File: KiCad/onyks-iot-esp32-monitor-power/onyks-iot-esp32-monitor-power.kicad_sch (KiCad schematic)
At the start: 42 parts, among them J1 Uart_con, J2 Jtag_con, J3 Conn_01x06, J4 Screw_Terminal_01x01, J5 Screw_Terminal_01x01, J6 Screw_Terminal_01x02, J7 Conn_01x02, K1 SANYOU_SRD_Form_C, Q1 SS8050, Q2 SS8050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

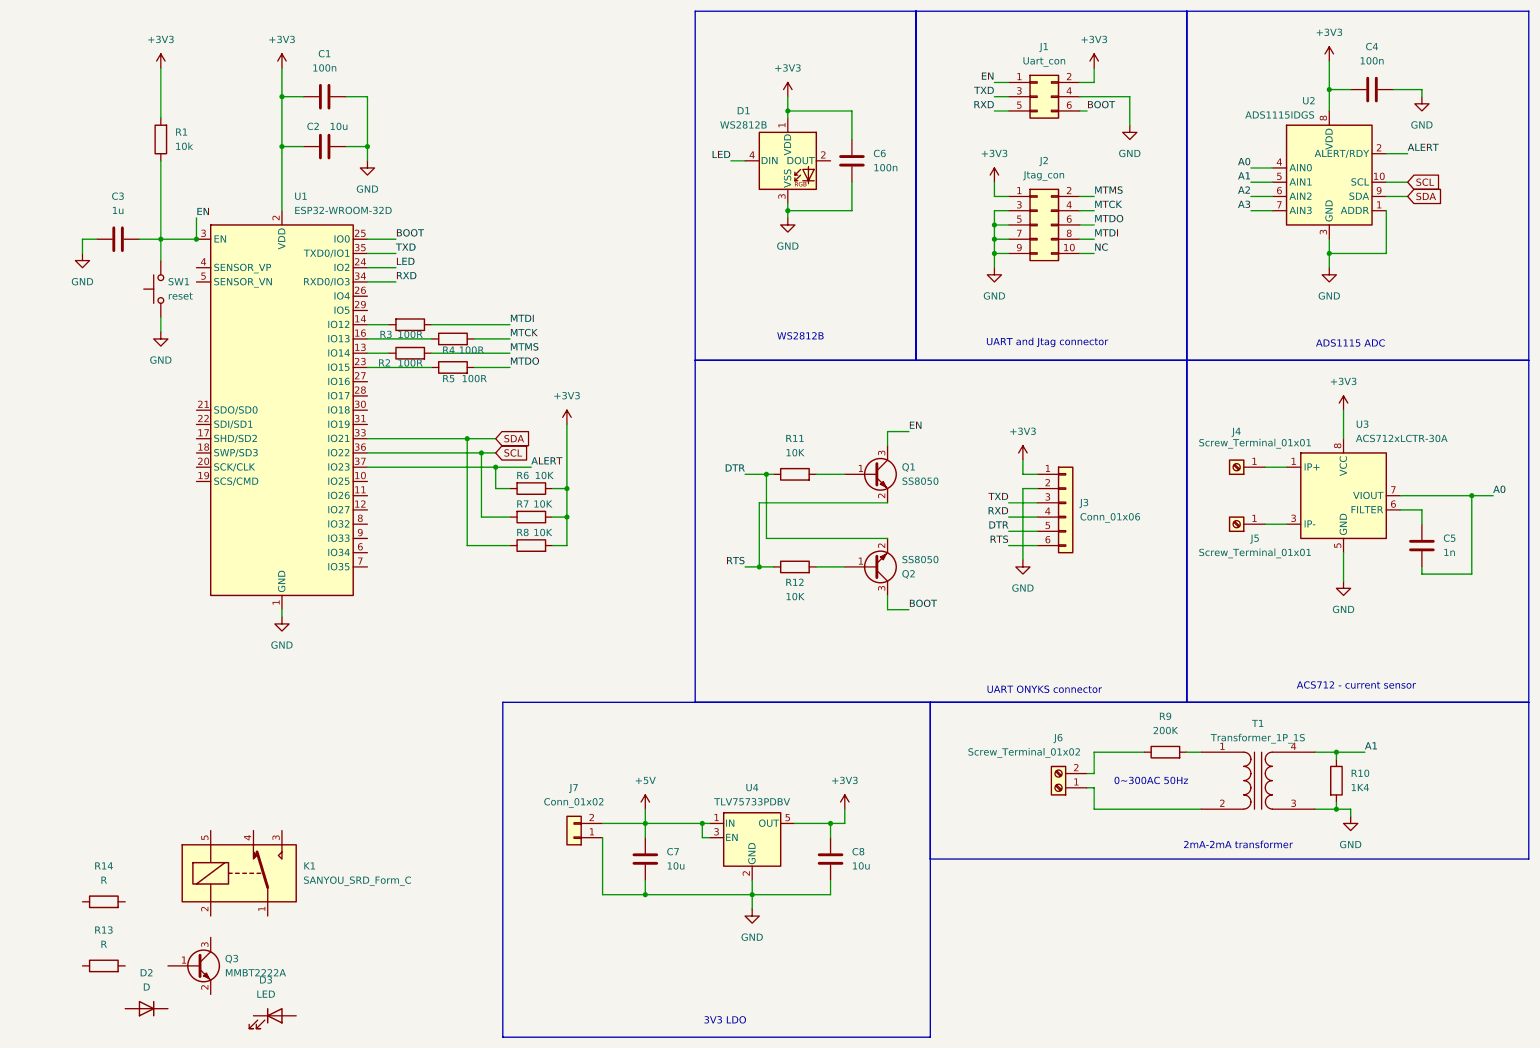
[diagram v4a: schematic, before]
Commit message: Add relay and 5x extra free GPIO; sheme V1.1
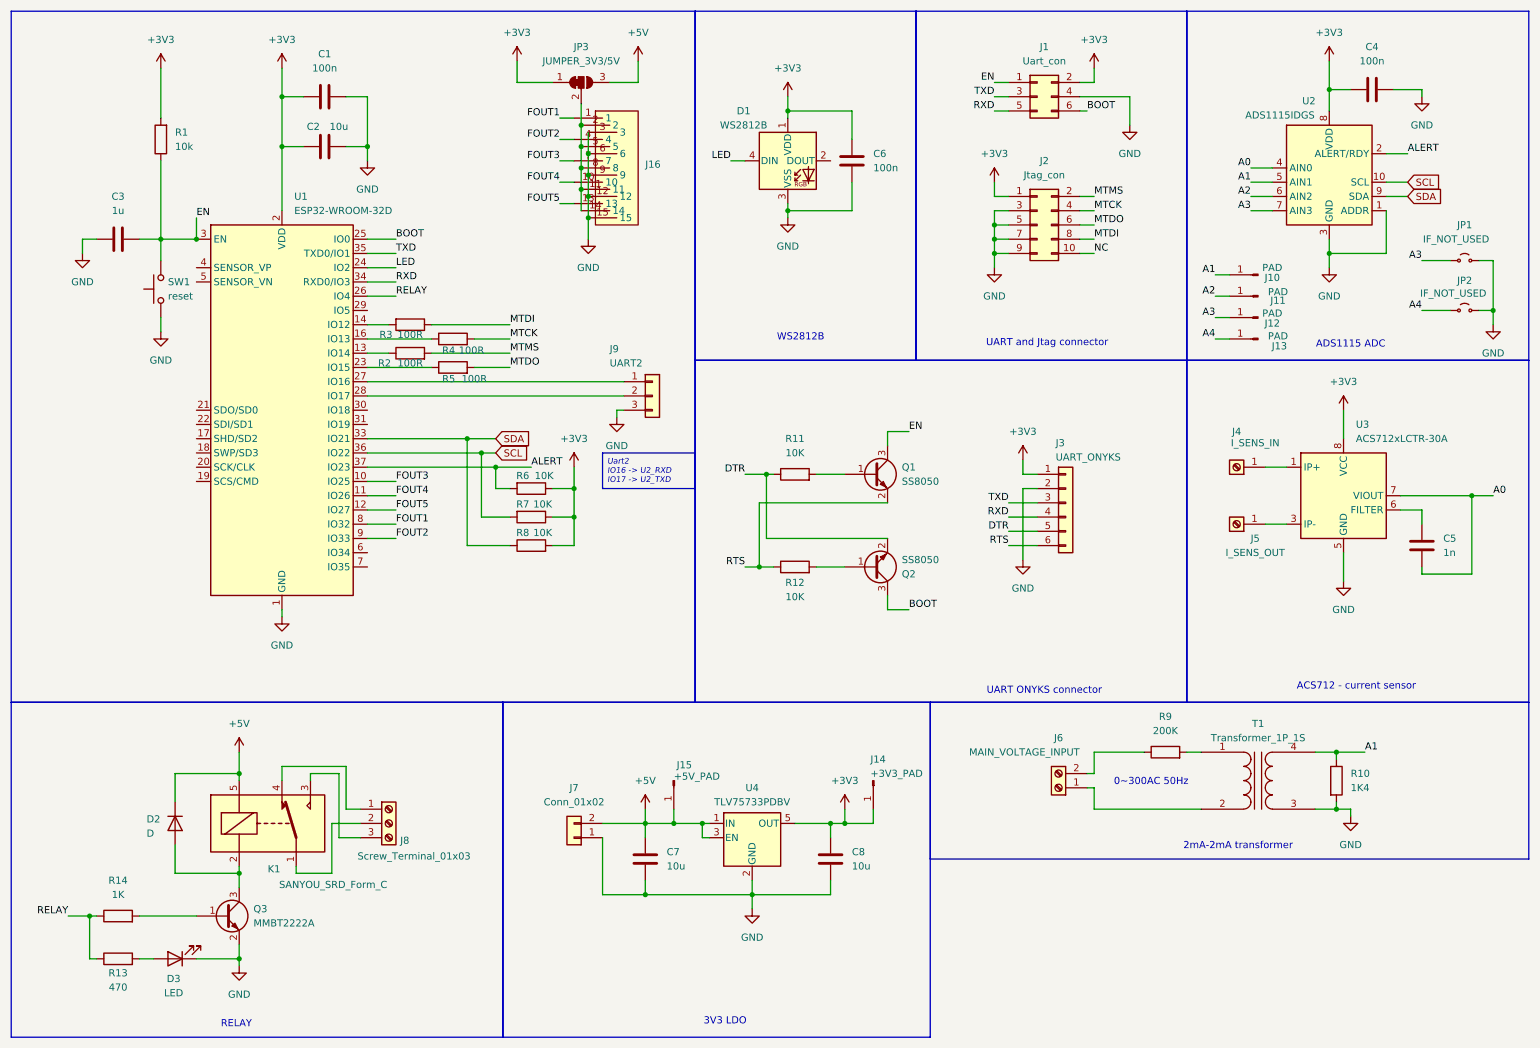
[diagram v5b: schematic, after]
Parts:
- added J10, J11, J12, J13: PAD, TestPoint:TestPoint_Pad_D1.0mm, symbol Connector:Conn_01x01_Pin
- added J14: +3V3_PAD, TestPoint:TestPoint_Pad_D1.5mm, symbol Connector:Conn_01x01_Pin
- added J15: +5V_PAD, TestPoint:TestPoint_Pad_D1.5mm, symbol Connector:Conn_01x01_Pin
- added J16: ~, macmysz:CONN_03x05, symbol macmysz:pin_03x05
- added J8: Screw_Terminal_01x03, TerminalBlock:TerminalBlock_bornier-3_P5.08mm, symbol Connector:Screw_Terminal_01x03
- added J9: UART2, Connector_PinHeader_2.54mm:PinHeader_1x03_P2.54mm_Vertical, symbol Connector_Generic:Conn_01x03
- added JP1, JP2: IF_NOT_USED, Jumper:SolderJumper-2_P1.3mm_Open_RoundedPad1.0x1.5mm, symbol Jumper:Jumper_2_Small_Open
- added JP3: JUMPER_3V3/5V, Jumper:SolderJumper-3_P1.3mm_Bridged12_RoundedPad1.0x1.5mm, symbol Jumper:SolderJumper_3_Bridged12
- D2: footprint (none) -> Diode_SMD:D_SMA
- D3: footprint (none) -> LED_SMD:LED_0603_1608Metric
- J3: value Conn_01x06 -> UART_ONYKS
- J4: value Screw_Terminal_01x01 -> I_SENS_IN
- J5: value Screw_Terminal_01x01 -> I_SENS_OUT
- J6: value Screw_Terminal_01x02 -> MAIN_VOLTAGE_INPUT
- R13: value R -> 470; footprint (none) -> Resistor_SMD:R_0805_2012Metric
- R14: value R -> 1K; footprint (none) -> Resistor_SMD:R_0805_2012Metric
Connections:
- net +3V3: now also J14.1 (Pin_1), JP3.1 (A)
- net +5V: now also D2.1 (K), K1.5, J15.1 (Pin_1), JP3.3 (B)
- net A1: now also J10.1 (Pin_1)
- net A2: now also J11.1 (Pin_1)
- net A3: now also J12.1 (Pin_1), JP1.1 (A)
- net GND: now also D3.1 (K), Q3.2 (E), J16.12, J16.15, J16.3, J16.6, J16.9, J9.3 (Pin_3), JP1.2 (B), JP2.2 (B)
- net at Q3.1 (B): now also R14.2
- net at Q3.3 (C): now also D2.2 (A), K1.2
- net at K1.1: now also J8.2 (Pin_2)
- net at K1.3: now also J8.3 (Pin_3)
- net at K1.4: now also J8.1 (Pin_1)
- net RELAY: now reaches R14.1
- net RELAY: now also R13.1, U1.26 (IO4)
- net at D3.2 (A): now also R13.2
- net FOUT3: now reaches U1.10 (IO25)
- net FOUT3: now also J16.7
- net FOUT4: now reaches U1.11 (IO26)
- net FOUT4: now also J16.10
- net FOUT5: now reaches U1.12 (IO27)
- net FOUT5: now also J16.13
- net at U1.27 (IO16): now also J9.1 (Pin_1)
- net at U1.28 (IO17): now also J9.2 (Pin_2)
- net FOUT1: now reaches U1.8 (IO32)
- net FOUT1: now also J16.1
- net FOUT2: now reaches U1.9 (IO33)
- net FOUT2: now also J16.4
- new net: J16.11, J16.14, J16.2, J16.5, J16.8, JP3.2 (C)
- new net A4: J13.1 (Pin_1), JP2.1 (A)
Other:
- note added: "RELAY"
- moved on the sheet: D2, D3, K1, Q3, R13, R14

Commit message: start editing pcb
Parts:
- removed R2, R3, R4, R5: 100R, Resistor_SMD:R_0805_2012Metric, symbol Device:R
- added RN1: 100, Resistor_SMD:R_Array_Concave_4x0603, symbol Device:R_Pack04
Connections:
- net A4 is gone; now on net A3: J13.1 (Pin_1), JP2.1 (A)
- net A0: now also J10.1 (Pin_1)
- net A1: now also J11.1 (Pin_1); no longer J10.1 (Pin_1)
- net A2: now also J12.1 (Pin_1), JP1.1 (A); no longer J11.1 (Pin_1)
- net A3: no longer J12.1 (Pin_1), JP1.1 (A)
- net MTCK: now also RN1.3 (R3.1)
- net MTDI: now also RN1.4 (R4.1)
- net MTDO: now also RN1.1 (R1.1)
- net MTMS: now also RN1.2 (R2.1)
- net at U1.23 (IO15): now also RN1.8 (R1.2)
- net at U1.13 (IO14): now also RN1.7 (R2.2)
- net at U1.14 (IO12): now also RN1.5 (R4.2)
- net at U1.16 (IO13): now also RN1.6 (R3.2)
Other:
- title: (none) -> ONYKS_iot_esp32_moitor_power

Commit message: edit pcb
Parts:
- removed J16: ~, macmysz:CONN_03x05, symbol macmysz:pin_03x05
- removed JP3: JUMPER_3V3/5V, Jumper:SolderJumper-3_P1.3mm_Bridged12_RoundedPad1.0x1.5mm, symbol Jumper:SolderJumper_3_Bridged12
- removed RN1: 100, Resistor_SMD:R_Array_Concave_4x0603, symbol Device:R_Pack04
- added J16: FOUT_conn, Connector_PinSocket_2.54mm:PinSocket_1x08_P2.54mm_Vertical, symbol Connector_Generic:Conn_01x08
- added J17: Ground, Connector_Wire:SolderWire-2sqmm_1x01_D2mm_OD3.9mm, symbol Connector:Screw_Terminal_01x01
- added RN1: 100, Resistor_SMD:R_Array_Concave_4x0603, symbol Device:R_Pack04_Split
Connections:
- net +3V3: now also J16.7 (Pin_7)
- net +5V: now also J16.8 (Pin_8)
- net FOUT1: now also J16.1 (Pin_1)
- net FOUT2: now also J16.2 (Pin_2)
- net FOUT3: now also J16.3 (Pin_3)
- net FOUT4: now also J16.4 (Pin_4)
- net FOUT5: now also J16.5 (Pin_5)
- net GND: now also J16.6 (Pin_6)
- net MTCK: now also RN1.2 (R2.1)
- net MTDI: now also RN1.4 (R4.1)
- net MTDO: now also RN1.3 (R3.1)
- net MTMS: now also RN1.1 (R1.1)
- net at U1.14 (IO12): now also RN1.5 (R4.2)
- net at U1.16 (IO13): now also RN1.7 (R2.2)
- net at U1.13 (IO14): now also RN1.8 (R1.2)
- net at U1.23 (IO15): now also RN1.6 (R3.2)
- new net Earth: J17.1 (Pin_1)

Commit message: schemat errors fix_1
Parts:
- C1, C4, C6: value 100n -> 100n/10V
- C2: value 10u -> 10u/10V
- C3: value 1u -> 1u/10V
- C5: value 1n -> 1n/10V
- C7, C8: value 10u -> 10u/25V
- T1: value Transformer_1P_1S -> 2mA-2mA transformer; Turns Ratio (none) -> 1000:1000
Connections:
- no-connect marks 0 -> 12
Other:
- note removed: "2mA-2mA transformer"
